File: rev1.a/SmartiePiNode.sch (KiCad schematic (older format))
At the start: 62 parts, among them CN1 USBMICROb, CN2 SWD, CN3 SX1238_TRX_HEADER, CN4 VIN, SW1 SW_PUSH, U1 ISL91127IR, U2 STM32L052_LQFP48, X1 abm10, X2 ABS25-32.768KHZ-6-T

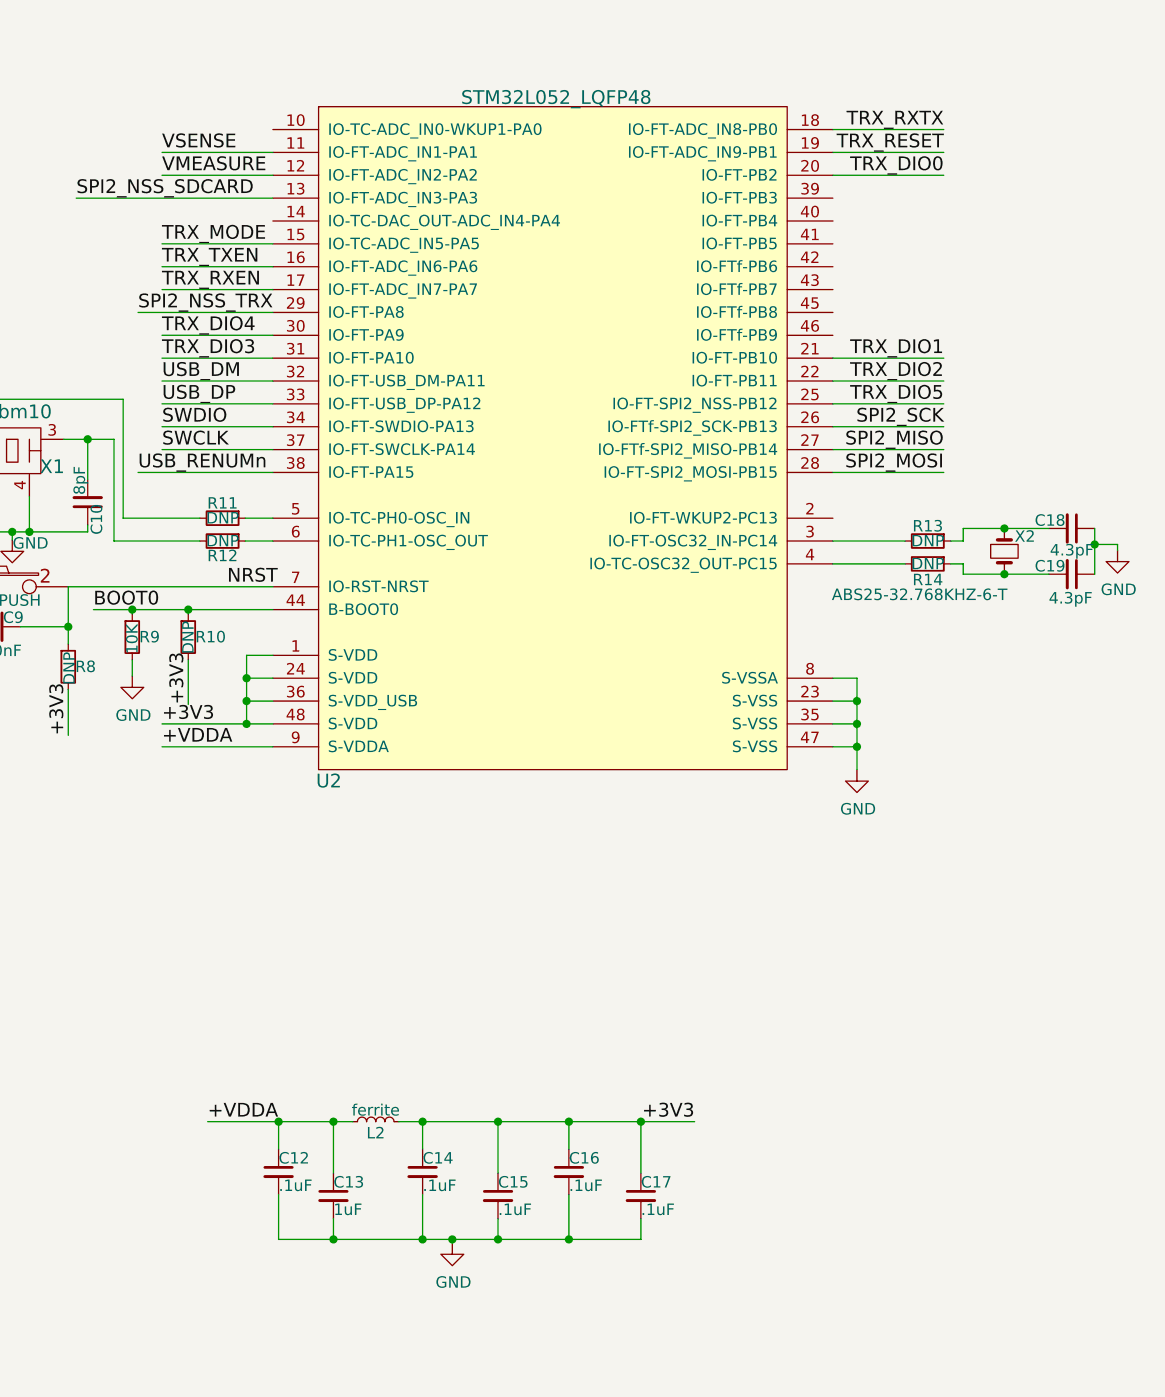
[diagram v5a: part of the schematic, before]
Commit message: created net for sensor gpio header
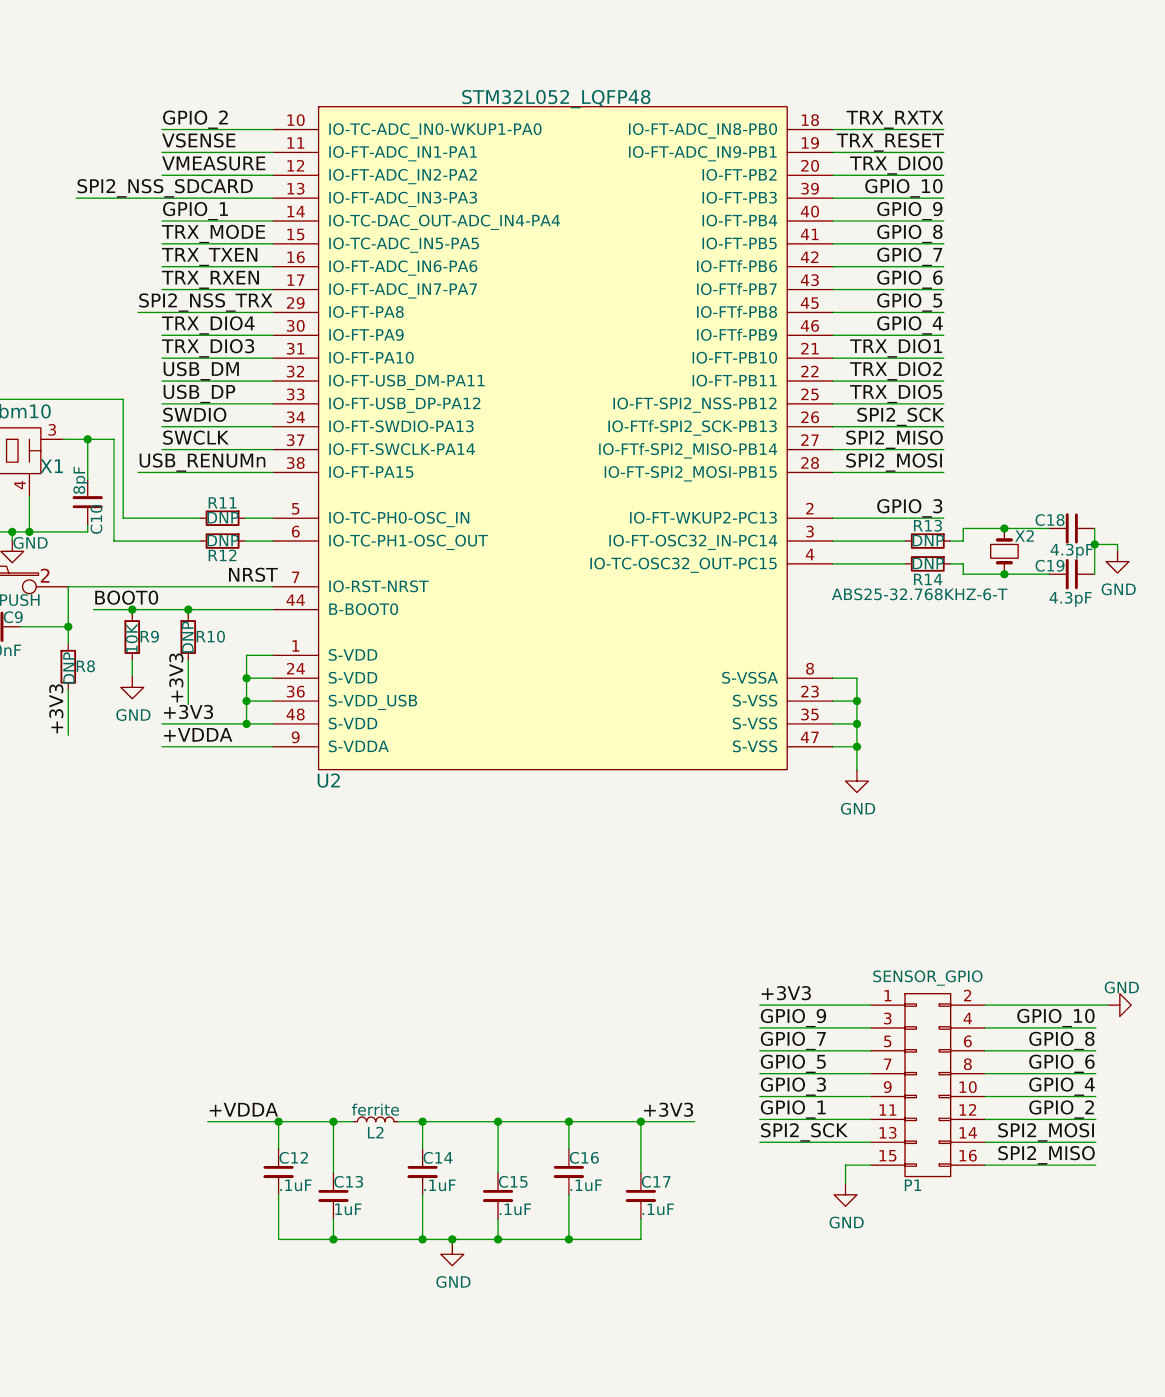
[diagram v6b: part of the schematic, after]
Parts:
- added P1: SENSOR_GPIO, Pin_Headers:Pin_Header_Straight_2x08, symbol CONN_02X08
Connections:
- net +3V3: now also P1.1 (P1)
- net GND: now also P1.15 (P15), P1.2 (P2)
- net SPI2_MISO: now also P1.16 (P16)
- net SPI2_MOSI: now also P1.14 (P14)
- net SPI2_SCK: now also P1.13 (P13)
- net GPIO_2: now reaches U2.10 (IO-TC-ADC_IN0-WKUP1-PA0)
- net GPIO_2: now also P1.12 (P12)
- net GPIO_1: now reaches U2.14 (IO-TC-DAC_OUT-ADC_IN4-PA4)
- net GPIO_1: now also P1.11 (P11)
- net GPIO_3: now reaches U2.2 (IO-FT-WKUP2-PC13)
- net GPIO_3: now also P1.9 (P9)
- net GPIO_10: now reaches U2.39 (IO-FT-PB3)
- net GPIO_10: now also P1.4 (P4)
- net GPIO_9: now reaches U2.40 (IO-FT-PB4)
- net GPIO_9: now also P1.3 (P3)
- net GPIO_8: now reaches U2.41 (IO-FT-PB5)
- net GPIO_8: now also P1.6 (P6)
- net GPIO_7: now reaches U2.42 (IO-FTf-PB6)
- net GPIO_7: now also P1.5 (P5)
- net GPIO_6: now reaches U2.43 (IO-FTf-PB7)
- net GPIO_6: now also P1.8 (P8)
- net GPIO_5: now reaches U2.45 (IO-FTf-PB8)
- net GPIO_5: now also P1.7 (P7)
- net GPIO_4: now reaches U2.46 (IO-FTf-PB9)
- net GPIO_4: now also P1.10 (P10)
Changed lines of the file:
@@
 $EndComp
 $Comp
-L GND #PWR01
+L GND #PWR11
 U 1 1 5B041A53
 P 3720 7315
-F 0 "#PWR01" H 3720 7065 50  0001 C CNN
+F 0 "#PWR11" H 3720 7065 50  0001 C CNN
 F 1 "GND" H 3725 7142 50  0000 C CNN
 F 2 "" H 3720 7315 50  0001 C CNN
@@
 $EndComp
 $Comp
-L GND #PWR02
+L GND #PWR16
 U 1 1 5B041F18
 P 4975 6485
-F 0 "#PWR02" H 4975 6235 50  0001 C CNN
+F 0 "#PWR16" H 4975 6235 50  0001 C CNN
 F 1 "GND" H 4980 6312 50  0000 C CNN
 F 2 "" H 4975 6485 50  0001 C CNN
@@
 $EndComp
 $Comp
-L GND #PWR03
+L GND #PWR17
 U 1 1 5B04234F
 P 5255 6485
-F 0 "#PWR03" H 5255 6235 50  0001 C CNN
+F 0 "#PWR17" H 5255 6235 50  0001 C CNN
 F 1 "GND" H 5260 6312 50  0000 C CNN
 F 2 "" H 5255 6485 50  0001 C CNN
@@
 $EndComp
 $Comp
-L GND #PWR04
+L GND #PWR19
 U 1 1 5B0423C8
 P 5530 6485
-F 0 "#PWR04" H 5530 6235 50  0001 C CNN
+F 0 "#PWR19" H 5530 6235 50  0001 C CNN
 F 1 "GND" H 5535 6312 50  0000 C CNN
 F 2 "" H 5530 6485 50  0001 C CNN
@@
 $EndComp
 $Comp
-L GND #PWR05
+L GND #PWR7
 U 1 1 5B04306E
 P 2340 6485
-F 0 "#PWR05" H 2340 6235 50  0001 C CNN
+F 0 "#PWR7" H 2340 6235 50  0001 C CNN
 F 1 "GND" H 2345 6312 50  0000 C CNN
 F 2 "" H 2340 6485 50  0001 C CNN
@@
 $EndComp
 $Comp
-L GND #PWR06
+L GND #PWR5
 U 1 1 5B04307C
 P 2060 6485
-F 0 "#PWR06" H 2060 6235 50  0001 C CNN
+F 0 "#PWR5" H 2060 6235 50  0001 C CNN
 F 1 "GND" H 2065 6312 50  0000 C CNN
 F 2 "" H 2060 6485 50  0001 C CNN
@@
 $EndComp
 $Comp
-L GND #PWR07
+L GND #PWR4
 U 1 1 5B04308A
 P 1785 6485
-F 0 "#PWR07" H 1785 6235 50  0001 C CNN
+F 0 "#PWR4" H 1785 6235 50  0001 C CNN
 F 1 "GND" H 1790 6312 50  0000 C CNN
 F 2 "" H 1785 6485 50  0001 C CNN
@@
 $EndComp
 $Comp
-L GND #PWR08
+L GND #PWR8
 U 1 1 5B043F5D
 P 2705 7280
-F 0 "#PWR08" H 2705 7030 50  0001 C CNN
+F 0 "#PWR8" H 2705 7030 50  0001 C CNN
 F 1 "GND" H 2710 7107 50  0000 C CNN
 F 2 "" H 2705 7280 50  0001 C CNN
@@
 $EndComp
 $Comp
-L GND #PWR09
+L GND #PWR13
 U 1 1 5B044D4C
 P 4485 7315
-F 0 "#PWR09" H 4485 7065 50  0001 C CNN
+F 0 "#PWR13" H 4485 7065 50  0001 C CNN
 F 1 "GND" H 4490 7142 50  0000 C CNN
 F 2 "" H 4485 7315 50  0001 C CNN
@@
 $EndComp
 $Comp
-L GND #PWR010
+L GND #PWR26
 U 1 1 5B06F6EF
 P 9930 3790
-F 0 "#PWR010" H 9930 3540 50  0001 C CNN
+F 0 "#PWR26" H 9930 3540 50  0001 C CNN
 F 1 "GND" H 9935 3617 50  0000 C CNN
 F 2 "" H 9930 3790 50  0001 C CNN
@@
 $EndComp
 $Comp
-L GND #PWR011
+L GND #PWR23
 U 1 1 5B0753BB
 P 6760 3380
-F 0 "#PWR011" H 6760 3130 50  0001 C CNN
+F 0 "#PWR23" H 6760 3130 50  0001 C CNN
 F 1 "GND" H 6765 3207 50  0000 C CNN
 F 2 "" H 6760 3380 50  0001 C CNN
@@
 $EndComp
 $Comp
-L GND #PWR012
+L GND #PWR3
 U 1 1 5B081C3A
 P 1715 4725
-F 0 "#PWR012" H 1715 4475 50  0001 C CNN
+F 0 "#PWR3" H 1715 4475 50  0001 C CNN
 F 1 "GND" H 1720 4552 50  0000 C CNN
 F 2 "" H 1715 4725 50  0001 C CNN
@@
 $EndComp
 $Comp
-L GND #PWR013
+L GND #PWR21
 U 1 1 5B082DC4
 P 5880 3240
-F 0 "#PWR013" H 5880 2990 50  0001 C CNN
+F 0 "#PWR21" H 5880 2990 50  0001 C CNN
 F 1 "GND" H 5885 3067 50  0000 C CNN
 F 2 "" H 5880 3240 50  0001 C CNN
@@
 Connection ~ 10575 2935
 $Comp
-L GND #PWR014
+L GND #PWR28
 U 1 1 5B098D9A
 P 11070 2830
-F 0 "#PWR014" H 11070 2580 50  0001 C CNN
+F 0 "#PWR28" H 11070 2580 50  0001 C CNN
 F 1 "GND" H 11075 2657 50  0000 C CNN
 F 2 "" H 11070 2830 50  0001 C CNN
@@
 	2225 1540 2225 1670
 $Comp
-L GND #PWR015
+L GND #PWR6
 U 1 1 5B0A5E1E
 P 2225 1670
-F 0 "#PWR015" H 2225 1420 50  0001 C CNN
+F 0 "#PWR6" H 2225 1420 50  0001 C CNN
 F 1 "GND" H 2230 1497 50  0000 C CNN
 F 2 "" H 2225 1670 50  0001 C CNN
@@
 +3V3
 $Comp
-L GND #PWR016
+L GND #PWR9
 U 1 1 5B0AC996
 P 3070 1200
-F 0 "#PWR016" H 3070 950 50  0001 C CNN
+F 0 "#PWR9" H 3070 950 50  0001 C CNN
 F 1 "GND" H 3075 1027 50  0000 C CNN
 F 2 "" H 3070 1200 50  0001 C CNN
@@
 SPI2_SCK
 $Comp
-L GND #PWR017
+L GND #PWR10
 U 1 1 5B0AE690
 P 3070 1500
-F 0 "#PWR017" H 3070 1250 50  0001 C CNN
+F 0 "#PWR10" H 3070 1250 50  0001 C CNN
 F 1 "GND" H 3075 1327 50  0000 C CNN
 F 2 "" H 3070 1500 50  0001 C CNN
@@
 	4145 2100 4720 2100
 $Comp
-L GND #PWR018
+L GND #PWR14
 U 1 1 5B0AEB87
 P 4720 2100
-F 0 "#PWR018" H 4720 1850 50  0001 C CNN
+F 0 "#PWR14" H 4720 1850 50  0001 C CNN
 F 1 "GND" H 4725 1927 50  0000 C CNN
 F 2 "" H 4720 2100 50  0001 C CNN
@@
 	1625 3160 1695 3160
 $Comp
-L GND #PWR019
+L GND #PWR2
 U 1 1 5B0B10C1
 P 1695 3160
-F 0 "#PWR019" H 1695 2910 50  0001 C CNN
+F 0 "#PWR2" H 1695 2910 50  0001 C CNN
 F 1 "GND" H 1700 2987 50  0000 C CNN
 F 2 "" H 1695 3160 50  0001 C CNN
@@
 NRST
 $Comp
-L GND #PWR020
+L GND #PWR12
 U 1 1 5B0B8F14
 P 4200 3080
-F 0 "#PWR020" H 4200 2830 50  0001 C CNN
+F 0 "#PWR12" H 4200 2830 50  0001 C CNN
 F 1 "GND" H 4205 2907 50  0000 C CNN
 F 2 "" H 4200 3080 50  0001 C CNN
@@
 $EndComp
 $Comp
-L GND #PWR021
+L GND #PWR24
 U 1 1 5B0C38AE
 P 8160 5860
-F 0 "#PWR021" H 8160 5610 50  0001 C CNN
+F 0 "#PWR24" H 8160 5610 50  0001 C CNN
 F 1 "GND" H 8165 5687 50  0000 C CNN
 F 2 "" H 8160 5860 50  0001 C CNN
@@
 Connection ~ 6235 2750
 $Comp
-L GND #PWR022
+L GND #PWR22
 U 1 1 5B1AE42D
 P 6235 2785
-F 0 "#PWR022" H 6235 2535 50  0001 C CNN
+F 0 "#PWR22" H 6235 2535 50  0001 C CNN
 F 1 "GND" H 6315 2770 50  0000 C CNN
 F 2 "" H 6235 2785 50  0001 C CNN
@@
 	4855 4565 4855 5170
 $Comp
-L GND #PWR023
+L GND #PWR15
 U 1 1 5B1D46F6
 P 4855 5170
-F 0 "#PWR023" H 4855 4920 50  0001 C CNN
+F 0 "#PWR15" H 4855 4920 50  0001 C CNN
 F 1 "GND" H 4860 4997 50  0000 C CNN
 F 2 "" H 4855 5170 50  0001 C CNN
@@
 	1290 5510 1290 5615
 $Comp
-L GND #PWR024
+L GND #PWR1
 U 1 1 5B2467F2
 P 1290 5615
-F 0 "#PWR024" H 1290 5365 50  0001 C CNN
+F 0 "#PWR1" H 1290 5365 50  0001 C CNN
 F 1 "GND" H 1295 5442 50  0000 C CNN
 F 2 "" H 1290 5615 50  0001 C CNN
@@
 	5270 1400 5270 1525
 $Comp
-L GND #PWR025
+L GND #PWR18
 U 1 1 5B27DE3A
 P 5270 1525
-F 0 "#PWR025" H 5270 1275 50  0001 C CNN
+F 0 "#PWR18" H 5270 1275 50  0001 C CNN
 F 1 "GND" H 5275 1352 50  0000 C CNN
 F 2 "" H 5270 1525 50  0001 C CNN
@@
 	5740 1345 5740 1395
 $Comp
-L GND #PWR026
+L GND #PWR20
 U 1 1 5B2802E4
 P 5740 1395
-F 0 "#PWR026" H 5740 1145 50  0001 C CNN
+F 0 "#PWR20" H 5740 1145 50  0001 C CNN
 F 1 "GND" H 5745 1222 50  0000 C CNN
 F 2 "" H 5740 1395 50  0001 C CNN
@@
 Wire Wire Line
 	6515 1290 7375 1290
+$Comp
+L CONN_02X08 P1
+U 1 1 5B364EB8
+P 10240 5170
+F 0 "P1" H 10175 4730 50  0000 C CNN
+F 1 "SENSOR_GPIO" H 10240 5644 50  0000 C CNN
+F 2 "Pin_Headers:Pin_Header_Straight_2x08" H 10240 3970 50  0001 C CNN
+F 3 "" H 10240 3970 50  0001 C CNN
+	1    10240 5170
+	1    0    0    -1
+$EndComp
+Text Label 10975 5420 2    60   ~ 0
+SPI2_MOSI
+Wire Wire Line
+	10975 5420 10490 5420
+Text Label 10975 5520 2    60   ~ 0
+SPI2_MISO
+Wire Wire Line
+	10975 5520 10490 5520
+Text Label 9505 5420 0    60   ~ 0
+SPI2_SCK
+Wire Wire Line
+	9505 5420 9990 5420
+Wire Wire Line
+	9990 5520 9880 5520
+Wire Wire Line
+	9880 5520 9880 5600
+$Comp
+L GND #PWR25
+U 1 1 5B3670FD
+P 9880 5600
+F 0 "#PWR25" H 9880 5350 50  0001 C CNN
+F 1 "GND" H 9885 5427 50  0000 C CNN
+F 2 "" H 9880 5600 50  0001 C CNN
+F 3 "" H 9880 5600 50  0001 C CNN
+	1    9880 5600
+	1    0    0    -1
+$EndComp
+Text Label 9505 5320 0    60   ~ 0
+GPIO_1
+Wire Wire Line
+	9505 5320 9990 5320
+Text Label 9505 5220 0    60   ~ 0
+GPIO_3
+Wire Wire Line
+	9505 5220 9990 5220
+Text Label 9505 5120 0    60   ~ 0
+GPIO_5
+Wire Wire Line
+	9505 5120 9990 5120
+Text Label 9505 5020 0    60   ~ 0
+GPIO_7
+Wire Wire Line
+	9505 5020 9990 5020
+Text Label 9505 4920 0    60   ~ 0
+GPIO_9
+Wire Wire Line
+	9505 4920 9990 4920
+Wire Wire Line
+	9505 4820 9990 4820
+Text Label 10975 5320 2    60   ~ 0
+GPIO_2
+Wire Wire Line
+	10975 5320 10490 5320
+Text Label 10975 5220 2    60   ~ 0
+GPIO_4
+Wire Wire Line
+	10975 5220 10490 5220
+Text Label 10975 5120 2    60   ~ 0
+GPIO_6
+Wire Wire Line
+	10975 5120 10490 5120
+Text Label 10975 5020 2    60   ~ 0
+GPIO_8
+Wire Wire Line
+	10975 5020 10490 5020
+Text Label 10975 4920 2    60   ~ 0
+GPIO_10
+Wire Wire Line
+	10975 4920 10490 4920
+Wire Wire Line
+	10490 4820 11030 4820
+Text Label 9505 4820 0    60   ~ 0
++3V3
+$Comp
+L GND #PWR27
+U 1 1 5B379033
+P 11030 4820
+F 0 "#PWR27" H 11030 4570 50  0001 C CNN
+F 1 "GND" V 11105 4840 50  0000 R CNN
+F 2 "" H 11030 4820 50  0001 C CNN
+F 3 "" H 11030 4820 50  0001 C CNN
+	1    11030 4820
+	0    -1   -1   0
+$EndComp
+Text Label 6890 1390 0    60   ~ 0
+GPIO_1
+Wire Wire Line
+	6890 1390 7375 1390
+Text Label 6890 990  0    60   ~ 0
+GPIO_2
+Wire Wire Line
+	6890 990  7375 990
+Text Label 10310 2690 2    60   ~ 0
+GPIO_3
+Wire Wire Line
+	10310 2690 9825 2690
+Text Label 10310 1890 2    60   ~ 0
+GPIO_4
+Wire Wire Line
+	10310 1890 9825 1890
+Text Label 10310 1790 2    60   ~ 0
+GPIO_5
+Wire Wire Line
+	10310 1790 9825 1790
+Text Label 10310 1690 2    60   ~ 0
+GPIO_6
+Wire Wire Line
+	10310 1690 9825 1690
+Text Label 10310 1590 2    60   ~ 0
+GPIO_7
+Wire Wire Line
+	10310 1590 9825 1590
+Text Label 10310 1490 2    60   ~ 0
+GPIO_8
+Wire Wire Line
+	10310 1490 9825 1490
+Text Label 10310 1390 2    60   ~ 0
+GPIO_9
+Wire Wire Line
+	10310 1390 9825 1390
+Text Label 10310 1290 2    60   ~ 0
+GPIO_10
+Wire Wire Line
+	10310 1290 9825 1290
 $EndSCHEMATC
